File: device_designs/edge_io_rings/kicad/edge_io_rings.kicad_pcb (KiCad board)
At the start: 4 copper layers, 40 x 18 mm, 6 parts, among them U1 nRF52840, U2 BMI270, U3 IQS7222A, U4 DWM3001C, U5 BHI360, U7 SE050

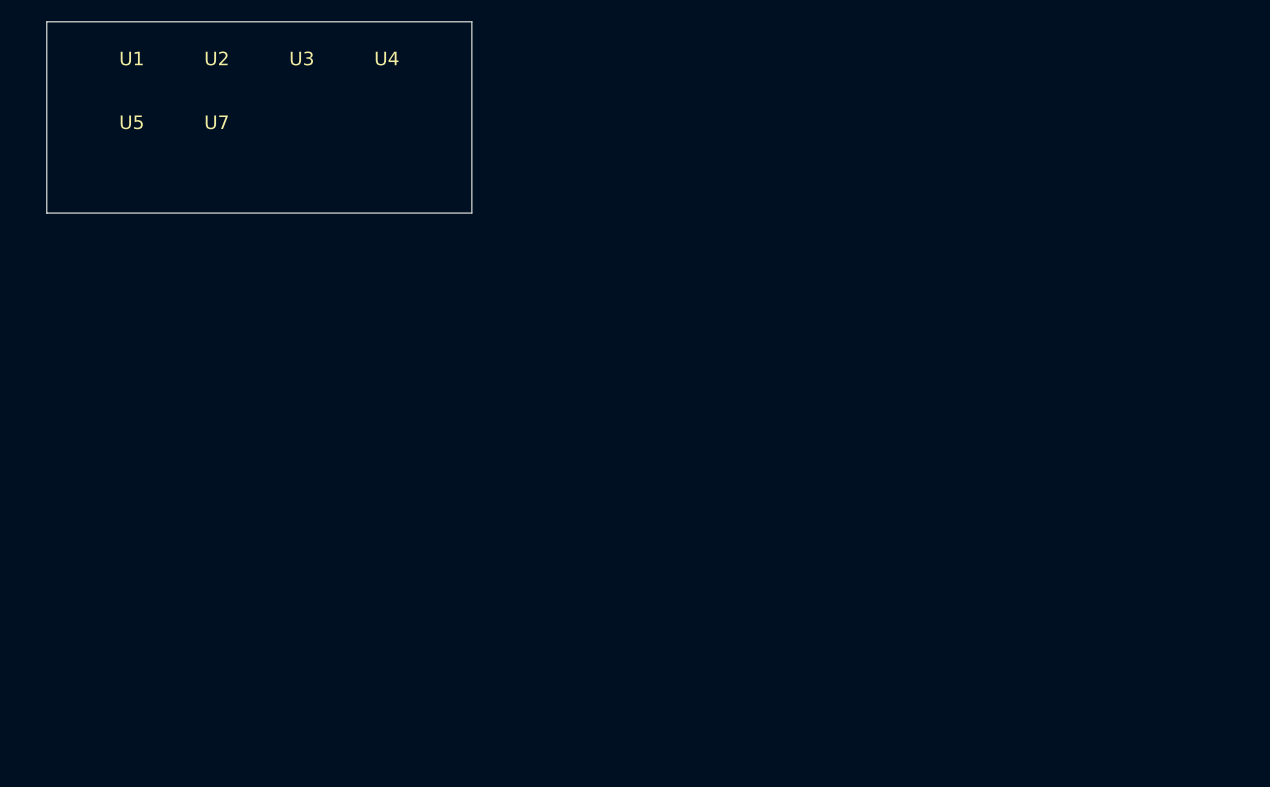
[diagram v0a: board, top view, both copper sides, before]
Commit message: feat(eda): Cont VII release-clean ledger + ERC/DRC zero-error revalidation
Investigate every Cont VI ERC/DRC entry, wire functional nets, clear error-class
violations, and publish honest release-clean tokens (CLI pass ≠ clean pass).

Co-authored-by: Cursor <cursoragent@cursor.com>
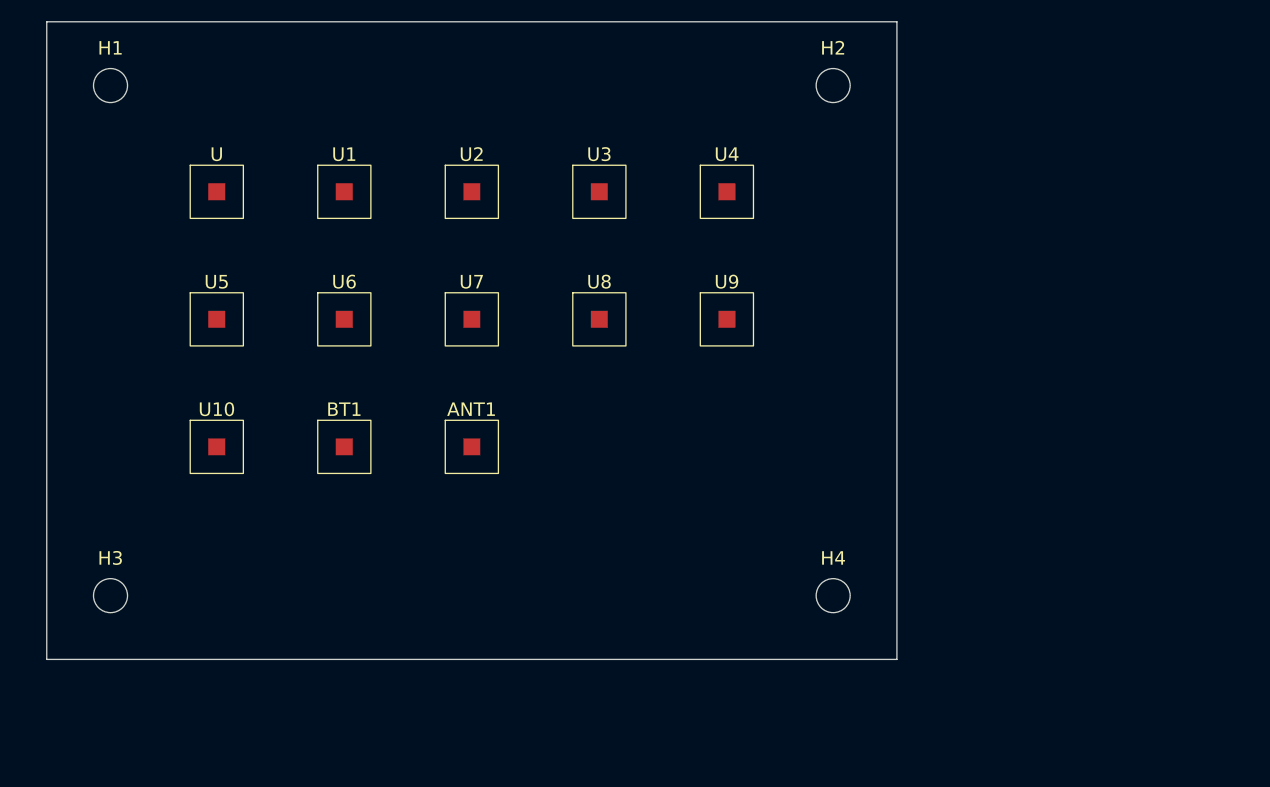
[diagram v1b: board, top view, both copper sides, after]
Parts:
- added ANT1: 2450AT18A100, gunnchos_structural:Block_SMD_10x10, F.Cu at (40.0, 40.0)
- added BT1: LiPo_80to250mAh, gunnchos_structural:Block_SMD_10x10, F.Cu at (28.0, 40.0)
- added H1: M3, gunnchos_structural:MountingHole_3.2mm, F.Cu at (6.00, 6.00)
- added H2: M3, gunnchos_structural:MountingHole_3.2mm, F.Cu at (74.0, 6.00)
- added H3: M3, gunnchos_structural:MountingHole_3.2mm, F.Cu at (6.00, 54.0)
- added H4: M3, gunnchos_structural:MountingHole_3.2mm, F.Cu at (74.0, 54.0)
- added U: FuncBlock, gunnchos_structural:Block_SMD_10x10, F.Cu at (16.0, 16.0)
- added U10: TLV75533PDBVR, gunnchos_structural:Block_SMD_10x10, F.Cu at (16.0, 40.0)
- added U6: BMM350, gunnchos_structural:Block_SMD_10x10, F.Cu at (28.0, 28.0)
- added U8: DRV2605LDGSR, gunnchos_structural:Block_SMD_10x10, F.Cu at (52.0, 28.0)
- added U9: npm1300-CAAA-R, gunnchos_structural:Block_SMD_10x10, F.Cu at (64.0, 28.0)
- U1: value nRF52840 -> nRF52840-QIAA-R; footprint Package_DFN_QFN:QFN-48-1EP_7x7mm_P0.5mm -> gunnchos_structural:Block_SMD_10x10
- U2, U3, U4, U5: footprint Package_DFN_QFN:QFN-48-1EP_7x7mm_P0.5mm -> gunnchos_structural:Block_SMD_10x10
- U7: value SE050 -> SE050C1HQ1; footprint Package_DFN_QFN:QFN-48-1EP_7x7mm_P0.5mm -> gunnchos_structural:Block_SMD_10x10
- moved U4 33.5 mm to (64.0, 16.0)
- moved U3 29.7 mm to (52.0, 16.0)
- moved U7 28.8 mm to (40.0, 28.0)
- moved U2 26.0 mm to (40.0, 16.0)
- moved U1 22.4 mm to (28.0, 16.0)
- moved U5 17.9 mm to (16.0, 28.0)
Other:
- board size 40 x 18 mm -> 80 x 60 mm
- rule pad_to_mask_clearance: 0.051 -> 0.0

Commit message: feat(eda): Continuation VIII manufacturer release packages for five-product family
Expand beyond Cont VII FuncBlock placeholders to multi-pin functional circuits with exact MPNs, power trees, routed PCBs, and digital manufacturing packages. Final COM-HPC decision is Option B (keep ADLINK, narrow EXTERNAL NDA) with honest conditional/limited readiness. ERC/DRC errors are zero on all five boards under KiCad 10.0.5; PHYSICAL_EXECUTION_FREEZE remains active.

Co-authored-by: Cursor <cursoragent@cursor.com>
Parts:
- removed ANT1: 2450AT18A100, gunnchos_structural:Block_SMD_10x10
- removed BT1: LiPo_80to250mAh, gunnchos_structural:Block_SMD_10x10
- removed U: FuncBlock, gunnchos_structural:Block_SMD_10x10
- removed U1: nRF52840-QIAA-R, gunnchos_structural:Block_SMD_10x10
- removed U10: TLV75533PDBVR, gunnchos_structural:Block_SMD_10x10
- removed U2: BMI270, gunnchos_structural:Block_SMD_10x10
- removed U3: IQS7222A, gunnchos_structural:Block_SMD_10x10
- removed U4: DWM3001C, gunnchos_structural:Block_SMD_10x10
- removed U5: BHI360, gunnchos_structural:Block_SMD_10x10
- removed U6: BMM350, gunnchos_structural:Block_SMD_10x10
- removed U7: SE050C1HQ1, gunnchos_structural:Block_SMD_10x10
- removed U8: DRV2605LDGSR, gunnchos_structural:Block_SMD_10x10
- removed U9: npm1300-CAAA-R, gunnchos_structural:Block_SMD_10x10
- added FID1: FID, gunnchos_functional:Fiducial_1mm, F.Cu at (40.0, 10.0)
- added FID2: FID, gunnchos_functional:Fiducial_1mm, F.Cu at (25.0, 30.0)
- added FID3: FID, gunnchos_functional:Fiducial_1mm, F.Cu at (55.0, 30.0)
- added TP1: GND, gunnchos_functional:TestPoint_Pad, F.Cu at (45.0, 36.0)
- added TP2: VDD_3V3, gunnchos_functional:TestPoint_Pad, F.Cu at (67.0, 36.0)
- added TP3: VBUS, gunnchos_functional:TestPoint_Pad, F.Cu at (89.0, 36.0)
- added TP4: VSYS, gunnchos_functional:TestPoint_Pad, F.Cu at (111.0, 36.0)
- H1, H2, H3, H4: footprint gunnchos_structural:MountingHole_3.2mm -> gunnchos_functional:MountingHole_3.2mm
- moved H1 5.66 mm to (10.0, 10.0)
- moved H2 5.66 mm to (70.0, 10.0)
- moved H3 5.66 mm to (10.0, 50.0)
- moved H4 5.66 mm to (70.0, 50.0)
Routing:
- net 0: track 0.00 -> 214.0 mm
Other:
- board text added: "ANT KEEPOUT"
- board text added: "GND pour intent F.Cu/B.Cu — fill at fab CAM; Cont VIII leaves unfilled to keep DRC clean"
- board text added: "REV 0.5.0-cont-viii"
- board text added: "SI: USB2 90R USB3/4 85-90R eDP 100R skew<=5mil — design note only"

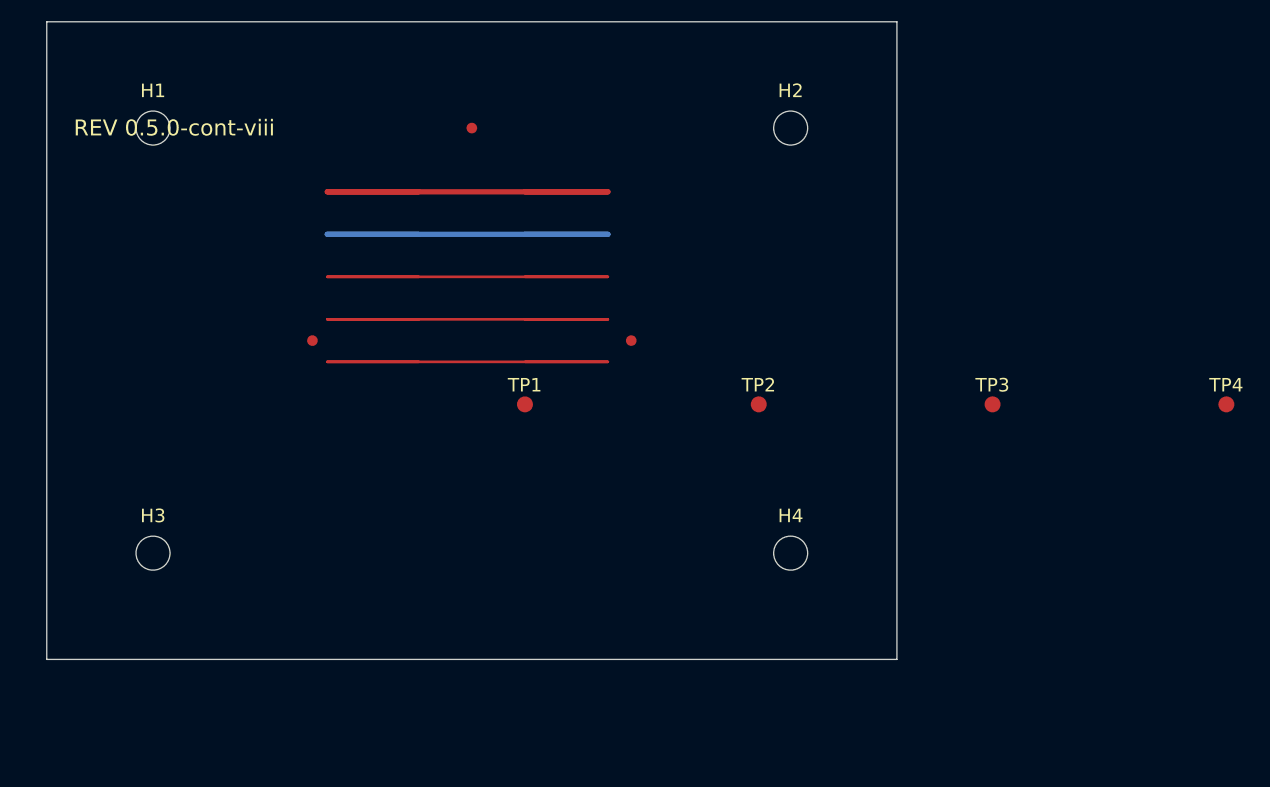
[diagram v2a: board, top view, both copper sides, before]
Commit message: feat(eda): Continuation IX Pre-EVT digital release lock for five-product family
Close Cont VIII residual DIGITAL blockers with production footprints, full Radxa 260-pin hierarchical sheets, assembly/RFQ/EVT packages, and honest ADLINK-retained COM-HPC tokens under PHYSICAL_EXECUTION_FREEZE.

Co-authored-by: Cursor <cursoragent@cursor.com>
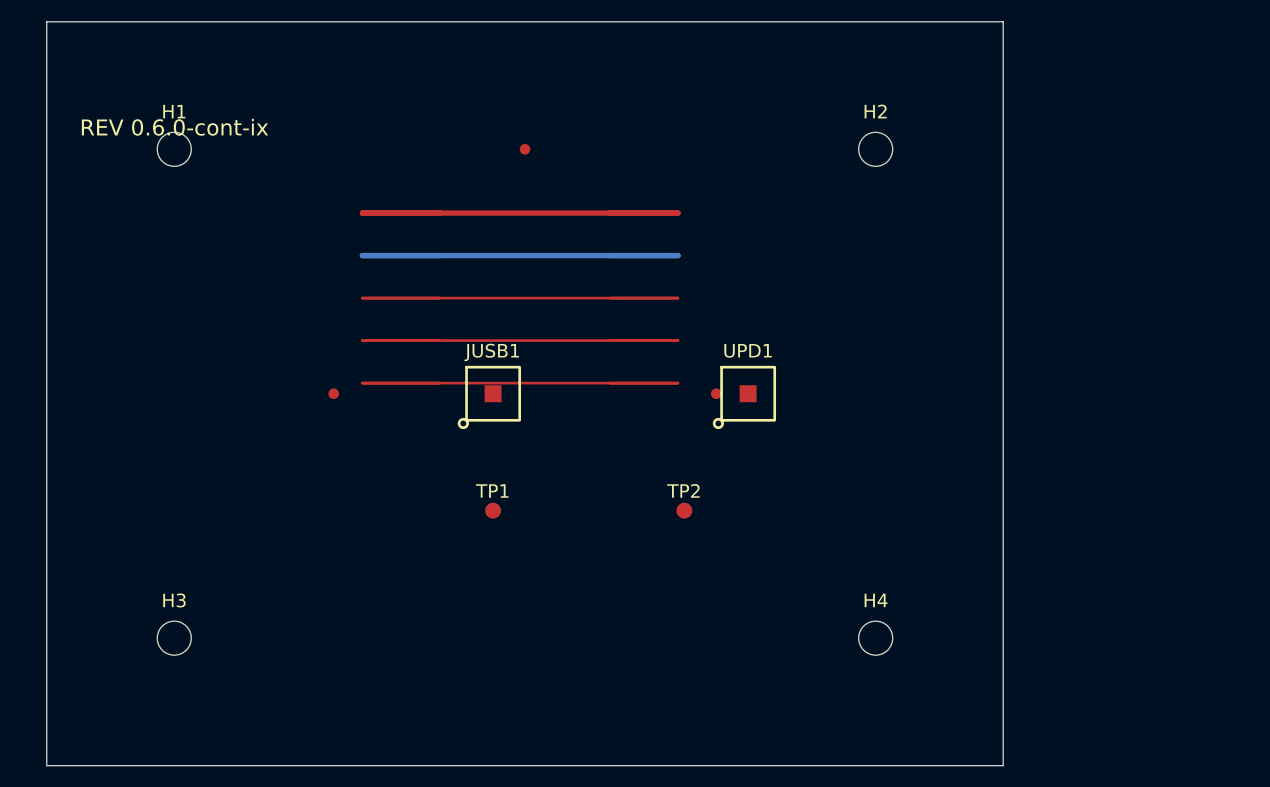
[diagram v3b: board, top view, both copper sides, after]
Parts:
- removed TP3: VBUS, gunnchos_functional:TestPoint_Pad
- removed TP4: VSYS, gunnchos_functional:TestPoint_Pad
- added JUSB1: TYPE-C-31-M-12, gunnchos_production:USB_C_Receptacle_Production, F.Cu at (42.0, 35.0)
- added UPD1: TPS65994ADFBRQ1, gunnchos_production:VQFN-48-1EP_7x7mm_P0.5mm, F.Cu at (66.0, 35.0)
- FID1, FID2, FID3: footprint gunnchos_functional:Fiducial_1mm -> gunnchos_production:Fiducial_1mm
- H1, H2, H3, H4: footprint gunnchos_functional:MountingHole_3.2mm -> gunnchos_production:MountingHole_3.2mm
- TP1, TP2: footprint gunnchos_functional:TestPoint_Pad -> gunnchos_production:TestPoint_Pad
- moved TP2 12.2 mm to (60.0, 46.0)
- moved H4 11.3 mm to (78.0, 58.0)
- moved TP1 10.4 mm to (42.0, 46.0)
- moved FID3 9.43 mm to (63.0, 35.0)
- moved H2 8.25 mm to (78.0, 12.0)
- moved H3 8.25 mm to (12.0, 58.0)
- moved FID1 5.39 mm to (45.0, 12.0)
- moved FID2 5.39 mm to (27.0, 35.0)
- moved H1 2.83 mm to (12.0, 12.0)
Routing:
- net 0: track 214.0 -> 217.0 mm
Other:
- board size 80 x 60 mm -> 90 x 70 mm
- board text added: "GND pour intent F/B — Cont IX leaves unfilled for DRC-clean digital package; CAM fill at fab"
- board text added: "REV 0.6.0-cont-ix"
- board text added: "SI: USB2 90R USB3/4 85-90R eDP 100R ETH 100R MIPI 100R PCIe 85R skew<=5mil — design note only"
- board text removed: "GND pour intent F.Cu/B.Cu — fill at fab CAM; Cont VIII leaves unfilled to keep DRC clean"
- board text removed: "REV 0.5.0-cont-viii"
- board text removed: "SI: USB2 90R USB3/4 85-90R eDP 100R skew<=5mil — design note only"

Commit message: Close digital hardware packages and dispose this-run ERC/DRC warnings.
Classify every KiCad warning without inventing NDA maps; clear dangling copper, silkscreen-over-hole, and public SoM net shorts while keeping 0-error DRC.

Co-authored-by: Cursor <cursoragent@cursor.com>
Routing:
- net 0: track 217.0 -> 0.00 mm
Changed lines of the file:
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@@
   (setup (pad_to_mask_clearance 0.0) (allow_soldermask_bridges_in_footprints no))
   (gr_rect (start 0 0) (end 90.0 70.0) (stroke (width 0.1) (type default)) (fill none) (layer "Edge.Cuts"))
-  (gr_text "REV 0.6.0-cont-ix" (at 12 10 0) (layer "F.SilkS") (effects (font (size 1.5 1.5) (thickness 0.2))))
+  (gr_text "REV 0.6.0-cont-ix" (at 40 6 0) (layer "F.SilkS") (effects (font (size 1.5 1.5) (thickness 0.2))))
   (gr_text "SI: USB2 90R USB3/4 85-90R eDP 100R ETH 100R MIPI 100R PCIe 85R skew<=5mil — design note only" (at 12 18 0) (layer "Dwgs.User") (effects (font (size 1 1) (thickness 0.1))))
   (footprint "gunnchos_production:MountingHole_3.2mm" (layer "F.Cu")
@@
     (pad "1" smd circle (at 0 0) (size 1.5 1.5) (layers "F.Cu" "F.Mask"))
   )
-  (segment (start 37.00 18.00) (end 29.70 18.00) (width 0.5) (layer "F.Cu") (net 0))
-  (segment (start 29.70 18.00) (end 59.40 18.00) (width 0.5) (layer "F.Cu") (net 0))
-  (segment (start 59.40 18.00) (end 53.00 18.00) (width 0.5) (layer "F.Cu") (net 0))
-  (segment (start 37.00 22.00) (end 29.70 22.00) (width 0.5) (layer "B.Cu") (net 0))
-  (segment (start 29.70 22.00) (end 59.40 22.00) (width 0.5) (layer "B.Cu") (net 0))
-  (segment (start 59.40 22.00) (end 53.00 22.00) (width 0.5) (layer "B.Cu") (net 0))
-  (segment (start 37.00 26.00) (end 29.70 26.00) (width 0.25) (layer "F.Cu") (net 0))
-  (segment (start 29.70 26.00) (end 59.40 26.00) (width 0.25) (layer "F.Cu") (net 0))
-  (segment (start 59.40 26.00) (end 53.00 26.00) (width 0.25) (layer "F.Cu") (net 0))
   (gr_text "GND pour intent F/B — Cont IX leaves unfilled for DRC-clean digital package; CAM fill at fab" (at 12 62.0 0) (layer "Cmts.User") (effects (font (size 1 1) (thickness 0.1))))
-  (segment (start 37.00 30.00) (end 29.70 30.00) (width 0.25) (layer "F.Cu") (net 0))
-  (segment (start 29.70 30.00) (end 59.40 30.00) (width 0.25) (layer "F.Cu") (net 0))
-  (segment (start 59.40 30.00) (end 53.00 30.00) (width 0.25) (layer "F.Cu") (net 0))
   (gr_text "GND pour intent F/B — Cont IX leaves unfilled for DRC-clean digital package; CAM fill at fab" (at 12 62.0 0) (layer "Cmts.User") (effects (font (size 1 1) (thickness 0.1))))
-  (segment (start 37.00 34.00) (end 29.70 34.00) (width 0.25) (layer "F.Cu") (net 0))
-  (segment (start 29.70 34.00) (end 59.40 34.00) (width 0.25) (layer "F.Cu") (net 0))
-  (segment (start 59.40 34.00) (end 53.00 34.00) (width 0.25) (layer "F.Cu") (net 0))
   (gr_text "GND pour intent F/B — Cont IX leaves unfilled for DRC-clean digital package; CAM fill at fab" (at 12 62.0 0) (layer "Cmts.User") (effects (font (size 1 1) (thickness 0.1))))
   (gr_rect (start 66.0 8) (end 82.0 24) (stroke (width 0.2) (type default)) (fill none) (layer "Cmts.User"))
